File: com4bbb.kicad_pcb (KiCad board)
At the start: 4 copper layers, 54.6 x 86.4 mm, 57 parts, among them J101 RS485, J102 PWR, J201 USB_B_Micro, J202 JTAG, P8 BeagleBone_Black_Header, P9 BeagleBone_Black_Header, SW101 Reset, SW102 PWR, U101 SP3485EN, U102 WPMDH1100xx1S, U103 AT24C512C-SSHD-T, U201 USBLC6-2SC6, U202 ESP32-S3-WROOM-1

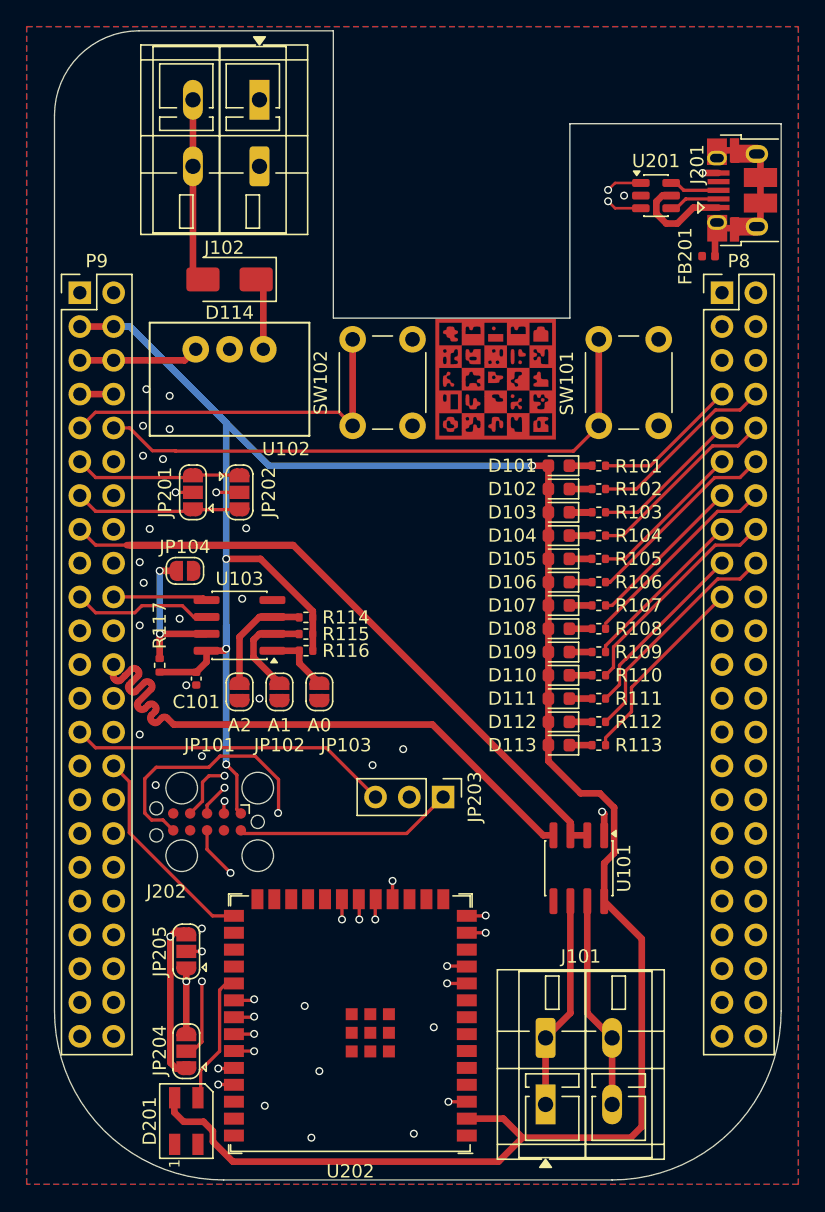
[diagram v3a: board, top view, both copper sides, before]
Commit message: Add RTC and secure memory
Signed-off-by: Benedikt Spranger <bene@eurovibes.org>
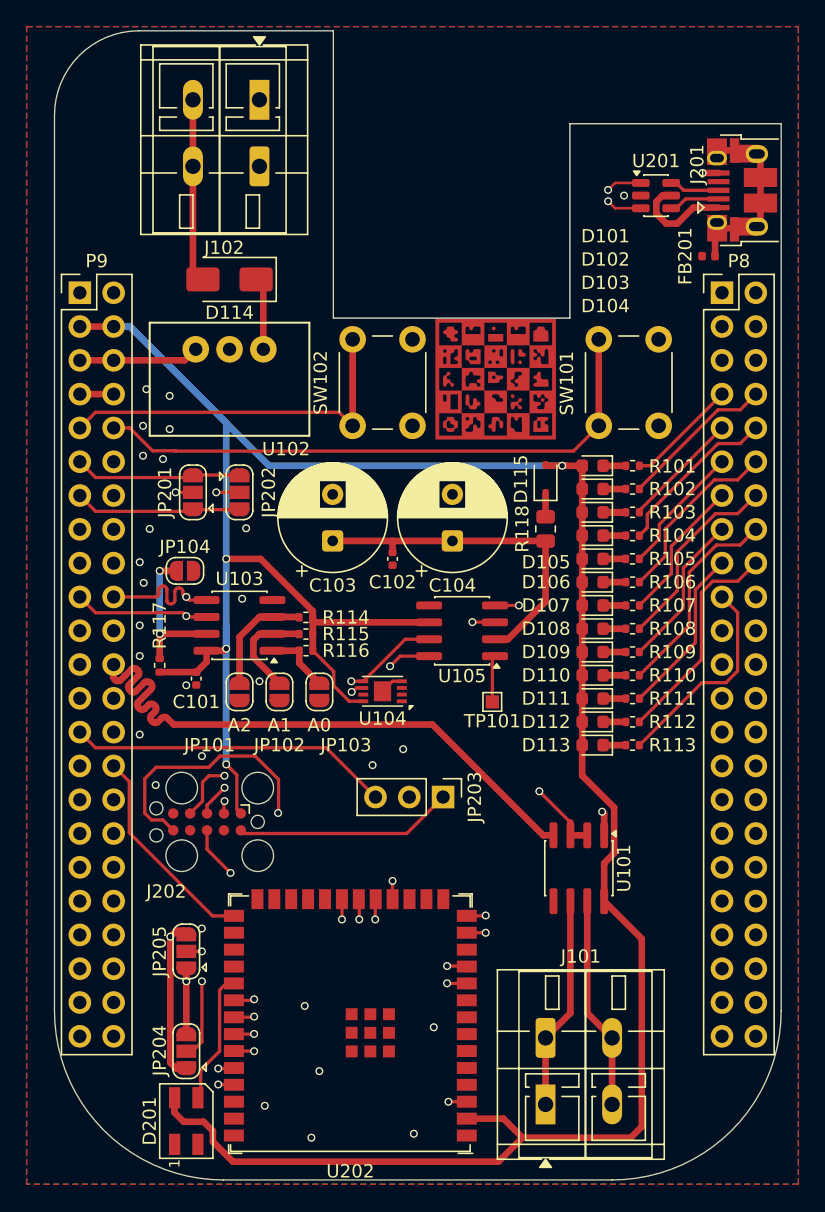
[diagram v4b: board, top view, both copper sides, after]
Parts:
- added C102: 100n, Capacitor_SMD:C_0402_1005Metric, F.Cu at (139.9, 82.4)
- added C103: 1F, Capacitor_THT:CP_Radial_D8.0mm_P3.50mm, F.Cu at (135.4, 81.0)
- added C104: 1F, Capacitor_THT:CP_Radial_D8.0mm_P3.50mm, F.Cu at (144.4, 81.0)
- added D115: 1N5819WS, Diode_SMD:D_SOD-323, F.Cu at (151.4, 76.4)
- added R118: 15, Resistor_SMD:R_0805_2012Metric, F.Cu at (151.4, 80.1)
- added TP101: 32kHz, TestPoint:TestPoint_Pad_1.0x1.0mm, F.Cu at (147.4, 93.1)
- added U104: ATECC608A-MAHDA, Package_DFN_QFN:DFN-8-1EP_3x2mm_P0.5mm_EP1.3x1.5mm, F.Cu at (139.1, 92.3)
- added U105: DS3231MZ, Package_SO:SOIC-8_3.9x4.9mm_P1.27mm, F.Cu at (145.1, 87.8)
- U102: value WPMDH1100xx1S -> R-78K5.0-0.5
- moved R105 2.54 mm to (157.9, 82.4)
- moved D101 2.54 mm to (154.9, 75.4)
- moved D102 2.54 mm to (154.9, 77.1)
- moved D103 2.54 mm to (154.9, 78.9)
- moved D104 2.54 mm to (154.9, 80.6)
- moved D105 2.54 mm to (154.9, 82.4)
- moved D106 2.54 mm to (154.9, 84.1)
- moved D107 2.54 mm to (154.9, 85.9)
- moved D108 2.54 mm to (154.9, 87.6)
- moved D109 2.54 mm to (154.9, 89.4)
- moved D110 2.54 mm to (154.9, 91.1)
- moved D111 2.54 mm to (154.9, 92.9)
- moved D112 2.54 mm to (154.9, 94.6)
- moved D113 2.54 mm to (154.9, 96.4)
- moved R101 2.54 mm to (157.9, 75.4)
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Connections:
- P9 pad 14: unconnected-(P9-Pin_14-Pad14) -> /RTC_INT
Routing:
- net /RTC_INT: track 0.00 -> 32.6 mm, vias 0 -> 1
- net /Vbat: track 0.00 -> 26.4 mm
- net /SDA: track 7.08 -> 32.3 mm, vias 0 -> 2
- net /SCL: track 10.6 -> 33.1 mm, vias 0 -> 3
- net SYS_RESETN: track 44.5 -> 62.3 mm, vias 0 -> 1
- net +3V3: track 205.6 -> 222.5 mm
- net /GPIO_48: track 60.7 -> 49.2 mm, vias 0 -> 1
- net Net-(U105-32KHZ): track 0.00 -> 3.52 mm
- net /LED0: track 11.0 -> 8.44 mm
- net /LED1: track 14.2 -> 11.7 mm
- net /LED2: track 11.4 -> 8.91 mm
- net /LED3: track 14.6 -> 12.7 mm
- net /LED4: track 11.8 -> 9.88 mm
- net Net-(D115-K): track 0.00 -> 1.79 mm
- net GNDD: track 3.68 -> 5.44 mm
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
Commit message: Change jumper position
Signed-off-by: Benedikt Spranger <bene@eurovibes.org>
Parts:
- moved JP203 7.85 mm to (135.8, 99.9), turned to 90 degrees
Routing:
- net /ESP32/~{RST}: track 16.4 -> 8.76 mm
- net /GPIO_125: track 24.2 -> 26.4 mm
- net Net-(JP203-C): track 25.6 -> 27.0 mm
- net GNDD: vias 28 -> 31
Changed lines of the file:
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@@
 	(footprint "Connector_PinHeader_2.54mm:PinHeader_1x03_P2.54mm_Vertical"
 		(layer "F.Cu")
-		(at 143.6701 100.2824 -90)
+		(at 135.8301 99.8824 90)
 		(descr "Through hole straight pin header, 1x03, 2.54mm pitch, single row")
 		(tags "Through hole pin header THT 1x03 2.54mm single row")
@@
 		)
 		(property "Long Description" "Connector: pin strips; pin header; male; PIN: 3; THT; straight; 1x3"
-			(at 0 0 270)
+			(at 0 0 90)
 			(unlocked yes)
 			(layer "F.Fab")
@@
 		)
 		(property "Source" "TME"
-			(at 0 0 270)
+			(at 0 0 90)
 			(unlocked yes)
 			(layer "F.Fab")
@@
 		)
 		(property "SupplLink" "https://www.tme.eu/de/en/details/zl201-03g/pin-headers/connfly/ds1021-1-3sf11-b/"
-			(at 0 0 270)
+			(at 0 0 90)
 			(unlocked yes)
 			(layer "F.Fab")
@@
 		)
 		(property "digikey#" ""
-			(at 0 0 270)
+			(at 0 0 90)
 			(unlocked yes)
 			(layer "F.Fab")
@@
 		)
 		(property "tme#" "ZL201-03G"
-			(at 0 0 270)
+			(at 0 0 90)
 			(unlocked yes)
 			(layer "F.Fab")
@@
 		)
 		(property "assemble" "n"
-			(at 0 0 270)
+			(at 0 0 90)
 			(unlocked yes)
 			(layer "F.Fab")
@@
 		)
 		(property "MF" "CONNFLY"
-			(at 0 0 270)
+			(at 0 0 90)
 			(unlocked yes)
 			(layer "F.Fab")
@@
 		)
 		(property "MP" "DS1021-1*3SF11-B"
-			(at 0 0 270)
+			(at 0 0 90)
 			(unlocked yes)
 			(layer "F.Fab")
@@
 		(attr through_hole exclude_from_bom)
 		(fp_line
-			(start -1.38 6.46)
-			(end 1.38 6.46)
+			(start -1.38 -1.38)
+			(end 0 -1.38)
 			(stroke
 				(width 0.12)
@@
 		)
 		(fp_line
-			(start -1.38 1.27)
-			(end -1.38 6.46)
+			(start -1.38 0)
+			(end -1.38 -1.38)
 			(stroke
 				(width 0.12)
@@
 		)
 		(fp_line
-			(start -1.38 1.27)
-			(end 1.38 1.27)
+			(start 1.38 1.27)
+			(end 1.38 6.46)
 			(stroke
 				(width 0.12)
@@
 		)
 		(fp_line
-			(start 1.38 1.27)
-			(end 1.38 6.46)
+			(start -1.38 1.27)
+			(end 1.38 1.27)
 			(stroke
 				(width 0.12)
@@
 		)
 		(fp_line
-			(start -1.38 0)
-			(end -1.38 -1.38)
+			(start -1.38 1.27)
+			(end -1.38 6.46)
 			(stroke
 				(width 0.12)
@@
 		)
 		(fp_line
-			(start -1.38 -1.38)
-			(end 0 -1.38)
+			(start -1.38 6.46)
+			(end 1.38 6.46)
 			(stroke
 				(width 0.12)
@@
 		)
 		(fp_line
-			(start -1.77 6.85)
-			(end 1.77 6.85)
+			(start 1.77 -1.77)
+			(end -1.77 -1.77)
 			(stroke
 				(width 0.05)
@@
 		)
 		(fp_line
-			(start 1.77 6.85)
-			(end 1.77 -1.77)
+			(start -1.77 -1.77)
+			(end -1.77 6.85)
 			(stroke
 				(width 0.05)
@@
 		)
 		(fp_line
-			(start -1.77 -1.77)
-			(end -1.77 6.85)
+			(start 1.77 6.85)
+			(end 1.77 -1.77)
 			(stroke
 				(width 0.05)
@@
 		)
 		(fp_line
-			(start 1.77 -1.77)
-			(end -1.77 -1.77)
+			(start -1.77 6.85)
+			(end 1.77 6.85)
 			(stroke
 				(width 0.05)
@@
 		)
 		(fp_line
-			(start -1.27 6.35)
-			(end -1.27 -0.635)
+			(start 1.27 -1.27)
+			(end 1.27 6.35)
 			(stroke
 				(width 0.1)
@@
 		)
 		(fp_line
-			(start 1.27 6.35)
-			(end -1.27 6.35)
+			(start -0.635 -1.27)
+			(end 1.27 -1.27)
 			(stroke
 				(width 0.1)
@@
 		)
 		(fp_line
-			(start -0.635 -1.27)
-			(end 1.27 -1.27)
+			(start 1.27 6.35)
+			(end -1.27 6.35)
 			(stroke
 				(width 0.1)
@@
 		)
 		(fp_line
-			(start 1.27 -1.27)
-			(end 1.27 6.35)
+			(start -1.27 6.35)
+			(end -1.27 -0.635)
 			(stroke
 				(width 0.1)
@@
 		)
 		(pad "1" thru_hole rect
-			(at 0 0 270)
+			(at 0 0 90)
 			(size 1.7 1.7)
 			(drill 1)
@@
 		)
 		(pad "2" thru_hole circle
-			(at 0 2.54 270)
+			(at 0 2.54 90)
 			(size 1.7 1.7)
 			(drill 1)
@@
 		)
 		(pad "3" thru_hole circle
-			(at 0 5.08 270)
+			(at 0 5.08 90)
 			(size 1.7 1.7)
 			(drill 1)
@@
 	)
 	(via
+		(at 148.1201 107.8824)
+		(size 0.6)
+		(drill 0.4)
+		(layers "F.Cu" "B.Cu")
+		(free yes)
+		(net 1)
+	)
+	(via
 		(at 120.8701 95.5824)
 		(size 0.6)
@@
 	)
 	(via
+		(at 144.1201 101.1324)
+		(size 0.6)
+		(drill 0.4)
+		(layers "F.Cu" "B.Cu")
+		(free yes)
+		(net 1)
+	)
+	(via
 		(at 120.8701 82.6324)
 		(size 0.6)
@@
 	)
 	(via
+		(at 135.8701 104.8824)
+		(size 0.6)
+		(drill 0.4)
+		(layers "F.Cu" "B.Cu")
+		(free yes)
+		(net 1)
+	)
+	(via
 		(at 121.1201 72.3824)
 		(size 0.6)
@@
 	)
 	(via
-		(at 140.6701 96.6824)
+		(at 132.3701 97.6324)
 		(size 0.6)
 		(drill 0.4)
@@
 	)
 	(via
-		(at 138.3701 97.8824)
+		(at 137.3701 97.3824)
 		(size 0.6)
 		(drill 0.4)
@@
 	)
 	(segment
-		(start 143.6701 100.2824)
-		(end 140.9328 103.0197)
+		(start 132.6928 103.0197)
+		(end 135.8301 99.8824)
 		(width 0.25)
 		(layer "F.Cu")
@@
 	)
 	(segment
-		(start 128.7064 103.0197)
-		(end 128.4701 102.7834)
+		(start 128.4701 102.7834)
+		(end 128.7064 103.0197)
 		(width 0.25)
 		(layer "F.Cu")
@@
 	)
 	(segment
-		(start 140.9328 103.0197)
-		(end 128.7064 103.0197)
+		(start 128.7064 103.0197)
+		(end 132.6928 103.0197)
 		(width 0.25)
 		(layer "F.Cu")
@@
 	)
 	(segment
-		(start 116.3701 95.4024)
-		(end 117.5461 96.5784)
+		(start 117.5461 96.5784)
+		(end 137.6061 96.5784)
 		(width 0.25)
 		(layer "F.Cu")
@@
 	)
 	(segment
-		(start 134.8861 96.5784)
-		(end 138.5901 100.2824)
+		(start 137.6061 96.5784)
+		(end 140.9101 99.8824)
 		(width 0.25)
 		(layer "F.Cu")
@@
 	)
 	(segment
-		(start 117.5461 96.5784)
-		(end 134.8861 96.5784)
+		(start 116.3701 95.4024)
+		(end 117.5461 96.5784)
 		(width 0.25)
 		(layer "F.Cu")
@@
 	)
 	(segment
-		(start 141.1301 120.4424)
-		(end 143.8701 123.1824)
+		(start 144.0701 123.1824)
+		(end 139.2201 118.3324)
 		(width 0.25)
 		(layer "In2.Cu")
@@
 	)
 	(segment
-		(start 143.8701 123.1824)
-		(end 144.0701 123.1824)
+		(start 139.2201 100.7324)
+		(end 138.3701 99.8824)
 		(width 0.25)
 		(layer "In2.Cu")
@@
 	)
 	(segment
-		(start 141.1301 100.2824)
-		(end 141.1301 120.4424)
+		(start 139.2201 118.3324)
+		(end 139.2201 100.7324)
 		(width 0.25)
 		(layer "In2.Cu")
